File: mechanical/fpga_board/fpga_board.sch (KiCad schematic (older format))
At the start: 37 parts, among them J1 Conn_02x17_Odd_Even, J2 Conn_02x17_Odd_Even, J3 Conn_02x17_Odd_Even, J4 Conn_02x17_Odd_Even, J5 Conn_02x17_Odd_Even, J6 jtag, J7 Conn_02x03_Odd_Even, J8 Conn_02x12_Odd_Even, U1 XC6SLX16-FTG256

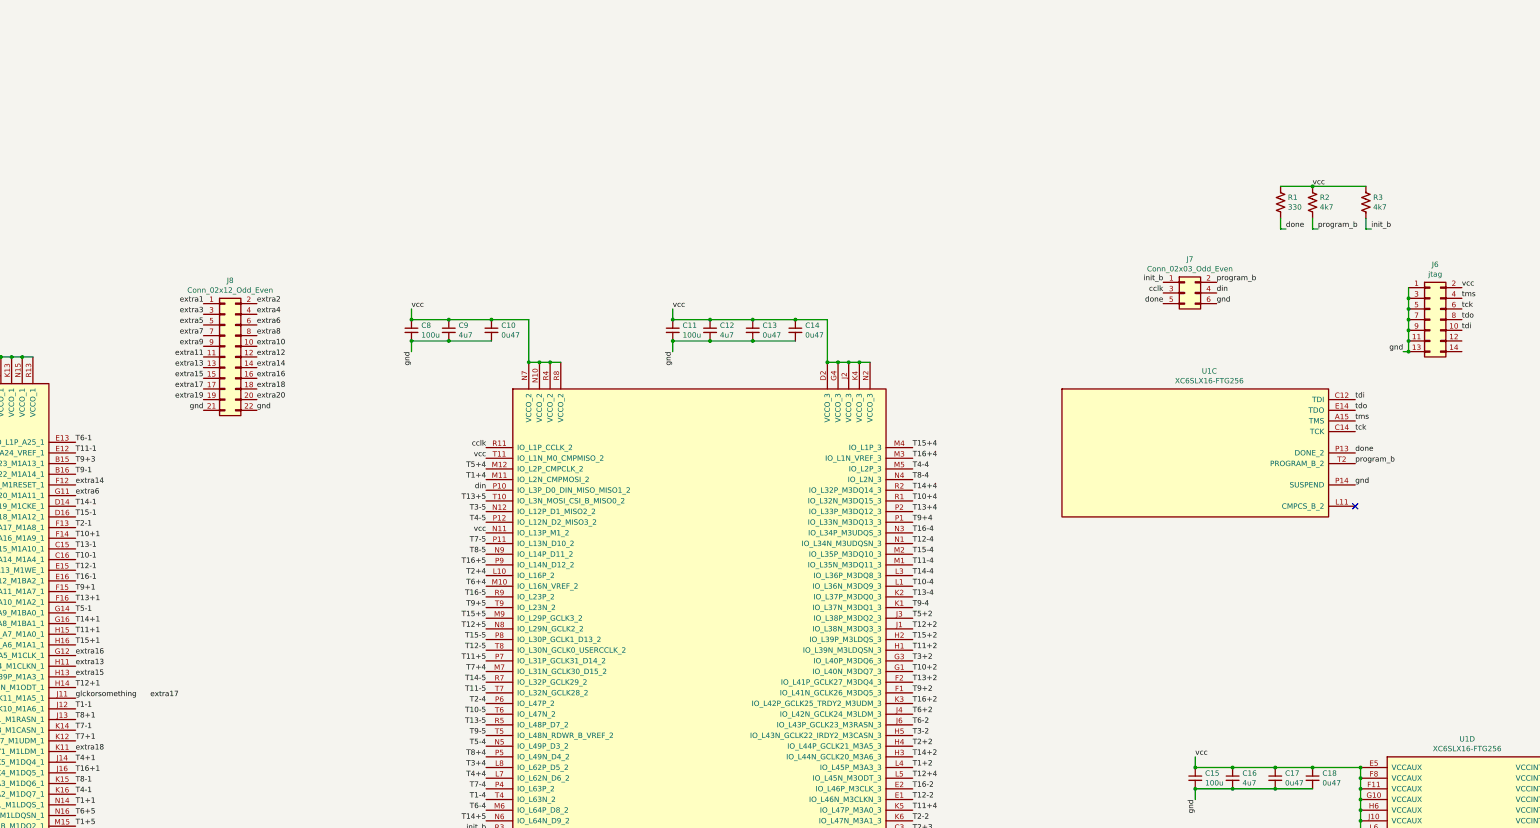
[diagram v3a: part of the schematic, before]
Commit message: Added linear regulators and oscillator
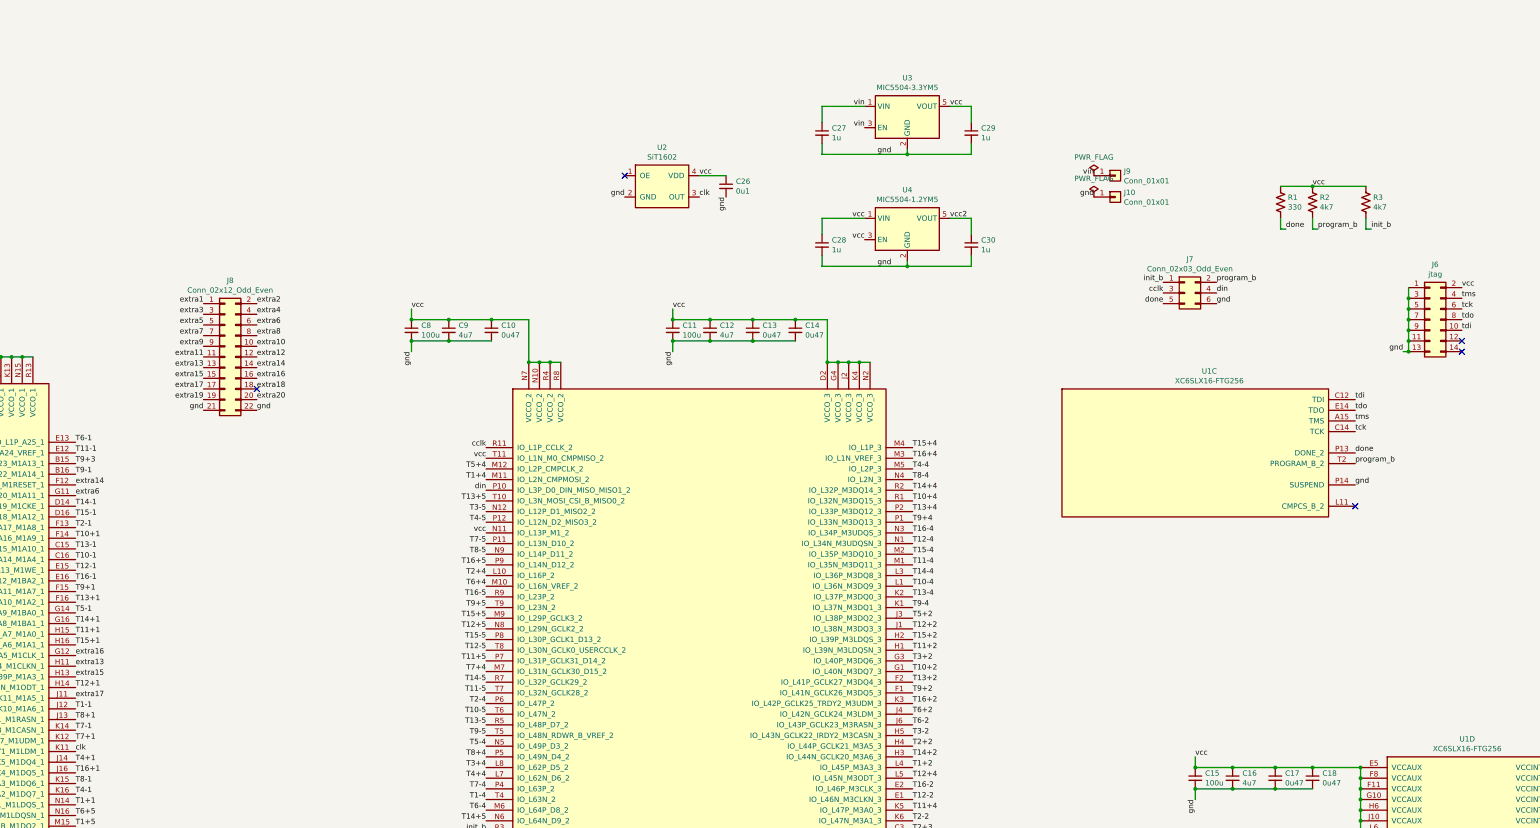
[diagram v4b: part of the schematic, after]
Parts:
- added C26: 0u1, Capacitor_SMD:C_0402_1005Metric, symbol Device:C_Small
- added C27, C28, C29, C30: 1u, Capacitor_SMD:C_0603_1608Metric, symbol Device:C_Small
- added J10, J9: Conn_01x01, Connector_Pin:Pin_D1.3mm_L11.0mm, symbol Connector_Generic:Conn_01x01
- added U2: SiT1602, FPGA_Board_Footprints:SiT1602_7_5, symbol FPGA_Board_Custom_Symbols:SiT1602
- added U3: MIC5504-3.3YM5, Package_TO_SOT_SMD:SOT-23-5, symbol Regulator_Linear:MIC5504-3.3YM5
- added U4: MIC5504-1.2YM5, Package_TO_SOT_SMD:SOT-23-5, symbol Regulator_Linear:MIC5504-1.2YM5
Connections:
- net glckorsomething is gone; now on net extra17: U1.J11 (IO_L40P_GCLK11_M1A5_1)
- net extra18: no longer U1.K11 (IO_L42N_GCLK6_TRDY1_M1LDM_1)
- net gnd: now also C26.2, C27.2, C28.2, C29.2, C30.2, J10.1 (Pin_1), U2.2 (GND), U3.2 (GND), U4.2 (GND)
- net vcc: now also C26.1, C28.1, C29.1, U2.4 (VDD), U3.5 (VOUT), U4.1 (VIN), U4.3 (EN)
- net vcc2: now also C30.1, U4.5 (VOUT)
- new net clk: U1.K11 (IO_L42N_GCLK6_TRDY1_M1LDM_1), U2.3 (OUT)
- new net vin: C27.1, J9.1 (Pin_1), U3.1 (VIN), U3.3 (EN)
- no-connect marks 11 -> 15
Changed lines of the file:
@@
 Text Label 8850 9300 0    50   ~ 0
 extra16
-Text Label 9550 9700 0    50   ~ 0
+Text Label 8850 9700 0    50   ~ 0
 extra17
-Text Label 8850 10200 0    50   ~ 0
-extra18
 Text Label 4850 10500 2    50   ~ 0
 extra19
@@
 Text Label 10550 7000 0    50   ~ 0
 gnd
-Text Label 8850 9700 0    50   ~ 0
-glckorsomething
+$Comp
+L Regulator_Linear:MIC5504-1.2YM5 U4
+U 1 1 60702C48
+P 16650 5300
+F 0 "U4" H 16650 5667 50  0000 C CNN
+F 1 "MIC5504-1.2YM5" H 16650 5576 50  0000 C CNN
+F 2 "Package_TO_SOT_SMD:SOT-23-5" H 16650 4900 50  0001 C CNN
+F 3 "http://ww1.microchip.com/downloads/en/DeviceDoc/MIC550X.pdf" H 16400 5550 50  0001 C CNN
+	1    16650 5300
+	1    0    0    -1
+$EndComp
+$Comp
+L Regulator_Linear:MIC5504-3.3YM5 U3
+U 1 1 6070665B
+P 16650 4250
+F 0 "U3" H 16650 4617 50  0000 C CNN
+F 1 "MIC5504-3.3YM5" H 16650 4526 50  0000 C CNN
+F 2 "Package_TO_SOT_SMD:SOT-23-5" H 16650 3850 50  0001 C CNN
+F 3 "http://ww1.microchip.com/downloads/en/DeviceDoc/MIC550X.pdf" H 16400 4500 50  0001 C CNN
+	1    16650 4250
+	1    0    0    -1
+$EndComp
+$Comp
+L FPGA_Board_Custom_Symbols:SiT1602 U2
+U 1 1 607143AE
+P 14350 4650
+F 0 "U2" H 14350 4765 50  0000 C CNN
+F 1 "SiT1602" H 14350 4674 50  0000 C CNN
+F 2 "FPGA_Board_Footprints:SiT1602_7_5" H 14350 4650 50  0001 C CNN
+F 3 "" H 14350 4650 50  0001 C CNN
+	1    14350 4650
+	1    0    0    -1
+$EndComp
+$Comp
+L Connector_Generic:Conn_01x01 J9
+U 1 1 60716400
+P 18600 4800
+F 0 "J9" H 18680 4842 50  0000 L CNN
+F 1 "Conn_01x01" H 18680 4751 50  0000 L CNN
+F 2 "Connector_Pin:Pin_D1.3mm_L11.0mm" H 18600 4800 50  0001 C CNN
+F 3 "~" H 18600 4800 50  0001 C CNN
+	1    18600 4800
+	1    0    0    -1
+$EndComp
+$Comp
+L Connector_Generic:Conn_01x01 J10
+U 1 1 60716DB4
+P 18600 5000
+F 0 "J10" H 18680 5042 50  0000 L CNN
+F 1 "Conn_01x01" H 18680 4951 50  0000 L CNN
+F 2 "Connector_Pin:Pin_D1.3mm_L11.0mm" H 18600 5000 50  0001 C CNN
+F 3 "~" H 18600 5000 50  0001 C CNN
+	1    18600 5000
+	1    0    0    -1
+$EndComp
+Text Label 18400 5000 2    50   ~ 0
+gnd
+Text Label 17050 5200 0    50   ~ 0
+vcc2
+Text Label 17050 4150 0    50   ~ 0
+vcc
+Text Label 16250 5200 2    50   ~ 0
+vcc
+Text Label 14000 5000 2    50   ~ 0
+gnd
+Text Label 14700 4800 0    50   ~ 0
+vcc
+NoConn ~ 14000 4800
+Text Label 16250 5400 2    50   ~ 0
+vcc
+Text Label 14700 5000 0    50   ~ 0
+clk
+$Comp
+L Device:C_Small C26
+U 1 1 6072E771
+P 14950 4900
+F 0 "C26" H 15042 4946 50  0000 L CNN
+F 1 "0u1" H 15042 4855 50  0000 L CNN
+F 2 "Capacitor_SMD:C_0402_1005Metric" H 14950 4900 50  0001 C CNN
+F 3 "~" H 14950 4900 50  0001 C CNN
+	1    14950 4900
+	1    0    0    -1
+$EndComp
+Text Label 14950 5000 3    50   ~ 0
+gnd
+Wire Wire Line
+	14700 4800 14950 4800
+Text Label 18400 4800 2    50   ~ 0
+vin
+Text Label 16250 4150 2    50   ~ 0
+vin
+Text Label 16250 4350 2    50   ~ 0
+vin
+$Comp
+L Device:C_Small C27
+U 1 1 607575F7
+P 15850 4400
+F 0 "C27" H 15942 4446 50  0000 L CNN
+F 1 "1u" H 15942 4355 50  0000 L CNN
+F 2 "Capacitor_SMD:C_0603_1608Metric" H 15850 4400 50  0001 C CNN
+F 3 "~" H 15850 4400 50  0001 C CNN
+	1    15850 4400
+	1    0    0    -1
+$EndComp
+Wire Wire Line
+	15850 4150 15850 4300
+Wire Wire Line
+	15850 4500 15850 4600
+Wire Wire Line
+	16650 4600 16650 4550
+Text Label 16500 4600 2    50   ~ 0
+gnd
+$Comp
+L Device:C_Small C29
+U 1 1 60762DD9
+P 17250 4400
+F 0 "C29" H 17342 4446 50  0000 L CNN
+F 1 "1u" H 17342 4355 50  0000 L CNN
+F 2 "Capacitor_SMD:C_0603_1608Metric" H 17250 4400 50  0001 C CNN
+F 3 "~" H 17250 4400 50  0001 C CNN
+	1    17250 4400
+	1    0    0    -1
+$EndComp
+Wire Wire Line
+	17250 4300 17250 4150
+Wire Wire Line
+	17250 4150 17050 4150
+Wire Wire Line
+	17250 4500 17250 4600
+Wire Wire Line
+	17250 4600 16650 4600
+Connection ~ 16650 4600
+Wire Wire Line
+	15850 4150 16250 4150
+Wire Wire Line
+	15850 4600 16650 4600
+$Comp
+L Device:C_Small C30
+U 1 1 607754DB
+P 17250 5450
+F 0 "C30" H 17342 5496 50  0000 L CNN
+F 1 "1u" H 17342 5405 50  0000 L CNN
+F 2 "Capacitor_SMD:C_0603_1608Metric" H 17250 5450 50  0001 C CNN
+F 3 "~" H 17250 5450 50  0001 C CNN
+	1    17250 5450
+	1    0    0    -1
+$EndComp
+Wire Wire Line
+	17250 5350 17250 5200
+Wire Wire Line
+	17250 5200 17050 5200
+Wire Wire Line
+	17250 5550 17250 5650
+Wire Wire Line
+	17250 5650 16650 5650
+Wire Wire Line
+	16650 5650 16650 5600
+$Comp
+L Device:C_Small C28
+U 1 1 60782D4C
+P 15850 5450
+F 0 "C28" H 15942 5496 50  0000 L CNN
+F 1 "1u" H 15942 5405 50  0000 L CNN
+F 2 "Capacitor_SMD:C_0603_1608Metric" H 15850 5450 50  0001 C CNN
+F 3 "~" H 15850 5450 50  0001 C CNN
+	1    15850 5450
+	1    0    0    -1
+$EndComp
+Wire Wire Line
+	15850 5350 15850 5200
+Wire Wire Line
+	15850 5200 16250 5200
+Wire Wire Line
+	15850 5550 15850 5650
+Wire Wire Line
+	15850 5650 16650 5650
+Connection ~ 16650 5650
+Text Label 16500 5650 2    50   ~ 0
+gnd
+Text Label 8850 10200 0    50   ~ 0
+clk
+NoConn ~ 10550 6800
+NoConn ~ 21850 6350
+NoConn ~ 21850 6450
+$Comp
+L power:PWR_FLAG #FLG0101
+U 1 1 608B9AF4
+P 18400 4800
+F 0 "#FLG0101" H 18400 4875 50  0001 C CNN
+F 1 "PWR_FLAG" H 18400 4973 50  0000 C CNN
+F 2 "" H 18400 4800 50  0001 C CNN
+F 3 "~" H 18400 4800 50  0001 C CNN
+	1    18400 4800
+	1    0    0    -1
+$EndComp
+$Comp
+L power:PWR_FLAG #FLG0102
+U 1 1 608B9E59
+P 18400 5000
+F 0 "#FLG0102" H 18400 5075 50  0001 C CNN
+F 1 "PWR_FLAG" H 18400 5173 50  0000 C CNN
+F 2 "" H 18400 5000 50  0001 C CNN
+F 3 "~" H 18400 5000 50  0001 C CNN
+	1    18400 5000
+	1    0    0    -1
+$EndComp
 $EndSCHEMATC
